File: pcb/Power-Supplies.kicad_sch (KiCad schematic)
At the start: 47 parts, among them U3 TPS560430, U4 TPS552872RYQR

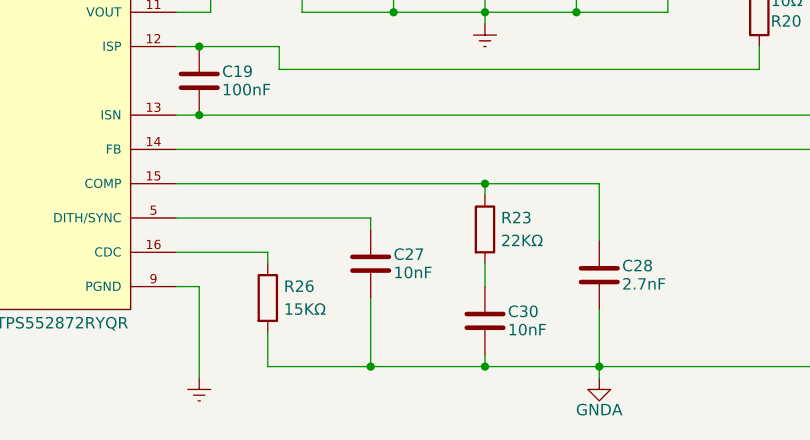
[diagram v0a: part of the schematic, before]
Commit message: Change R23 to 15KΩ
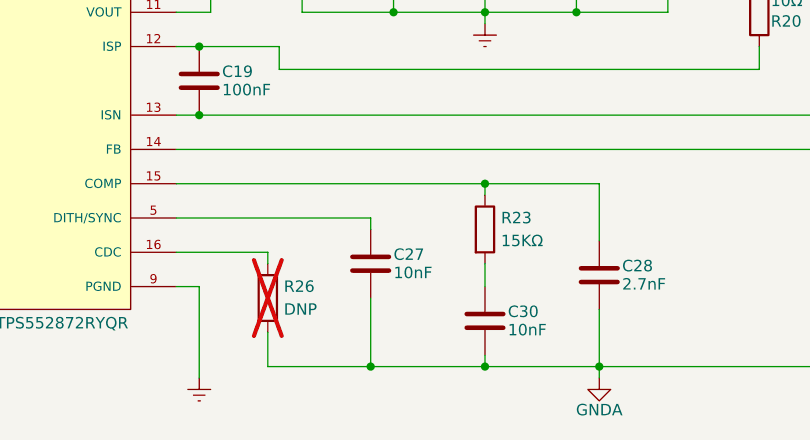
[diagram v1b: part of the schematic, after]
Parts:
- R23: value 22KΩ -> 15KΩ; Comment 22K Resistor -> 15K Resistor; LCSC C25768 -> C25539
- R26: value 15KΩ -> DNP; now not fitted
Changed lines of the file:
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@@
 			)
 		)
-		(property "Value" "22KΩ"
+		(property "Value" "15KΩ"
 			(at 203.708 133.35 0)
 			(effects
@@
 			)
 		)
-		(property "Description" "Resistor, 22KΩ, 62.5mW, 1%, 0402"
+		(property "Description" "Resistor, 15KΩ, 62.5mW, 1%, 0402"
 			(at 201.93 132.08 0)
 			(effects
@@
 			)
 		)
-		(property "Comment" "22K Resistor"
-			(at 201.93 132.08 0)
-			(effects
-				(font
-					(size 1.27 1.27)
-				)
-				(hide yes)
-			)
-		)
-		(property "LCSC" "C25768"
+		(property "Comment" "15K Resistor"
+			(at 201.93 132.08 0)
+			(effects
+				(font
+					(size 1.27 1.27)
+				)
+				(hide yes)
+			)
+		)
+		(property "LCSC" "C25539"
 			(at 201.93 132.08 0)
 			(effects
@@
 		(in_bom yes)
 		(on_board yes)
-		(dnp no)
+		(dnp yes)
 		(property "Reference" "R26"
 			(at 179.578 138.43 0)
@@
 			)
 		)
-		(property "Value" "15KΩ"
+		(property "Value" "DNP"
 			(at 179.578 140.97 0)
 			(effects
@@
 			)
 		)
-		(property "Description" "Resistor, 15KΩ, 62.5mW, 1%, 0402"
+		(property "Description" ""
 			(at 177.8 139.7 0)
 			(effects

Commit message: Fix last commit. R26 is DNP and R23 changed to 15kΩ.
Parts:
- R26: Comment 15K Resistor -> (none); LCSC C25539 -> (none)
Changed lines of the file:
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@@
 			)
 		)
-		(property "Description" ""
+		(property "Description" "Resistor, Do Not Populate, 0402"
 			(at 177.8 139.7 0)
 			(effects
@@
 			)
 		)
-		(property "Comment" "15K Resistor"
+		(property "Comment" ""
 			(at 177.8 139.7 0)
 			(effects
@@
 			)
 		)
-		(property "LCSC" "C25539"
+		(property "LCSC" ""
 			(at 177.8 139.7 0)
 			(effects
